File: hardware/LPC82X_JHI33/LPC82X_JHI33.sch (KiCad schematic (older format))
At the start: 24 parts, among them J1 LPC82XJHI33_LEFT, J2 LPC82XJHI33_RIGHT, J3 JTAG_2X05, U1 LPC824M201JHI33, Y1 12MHz

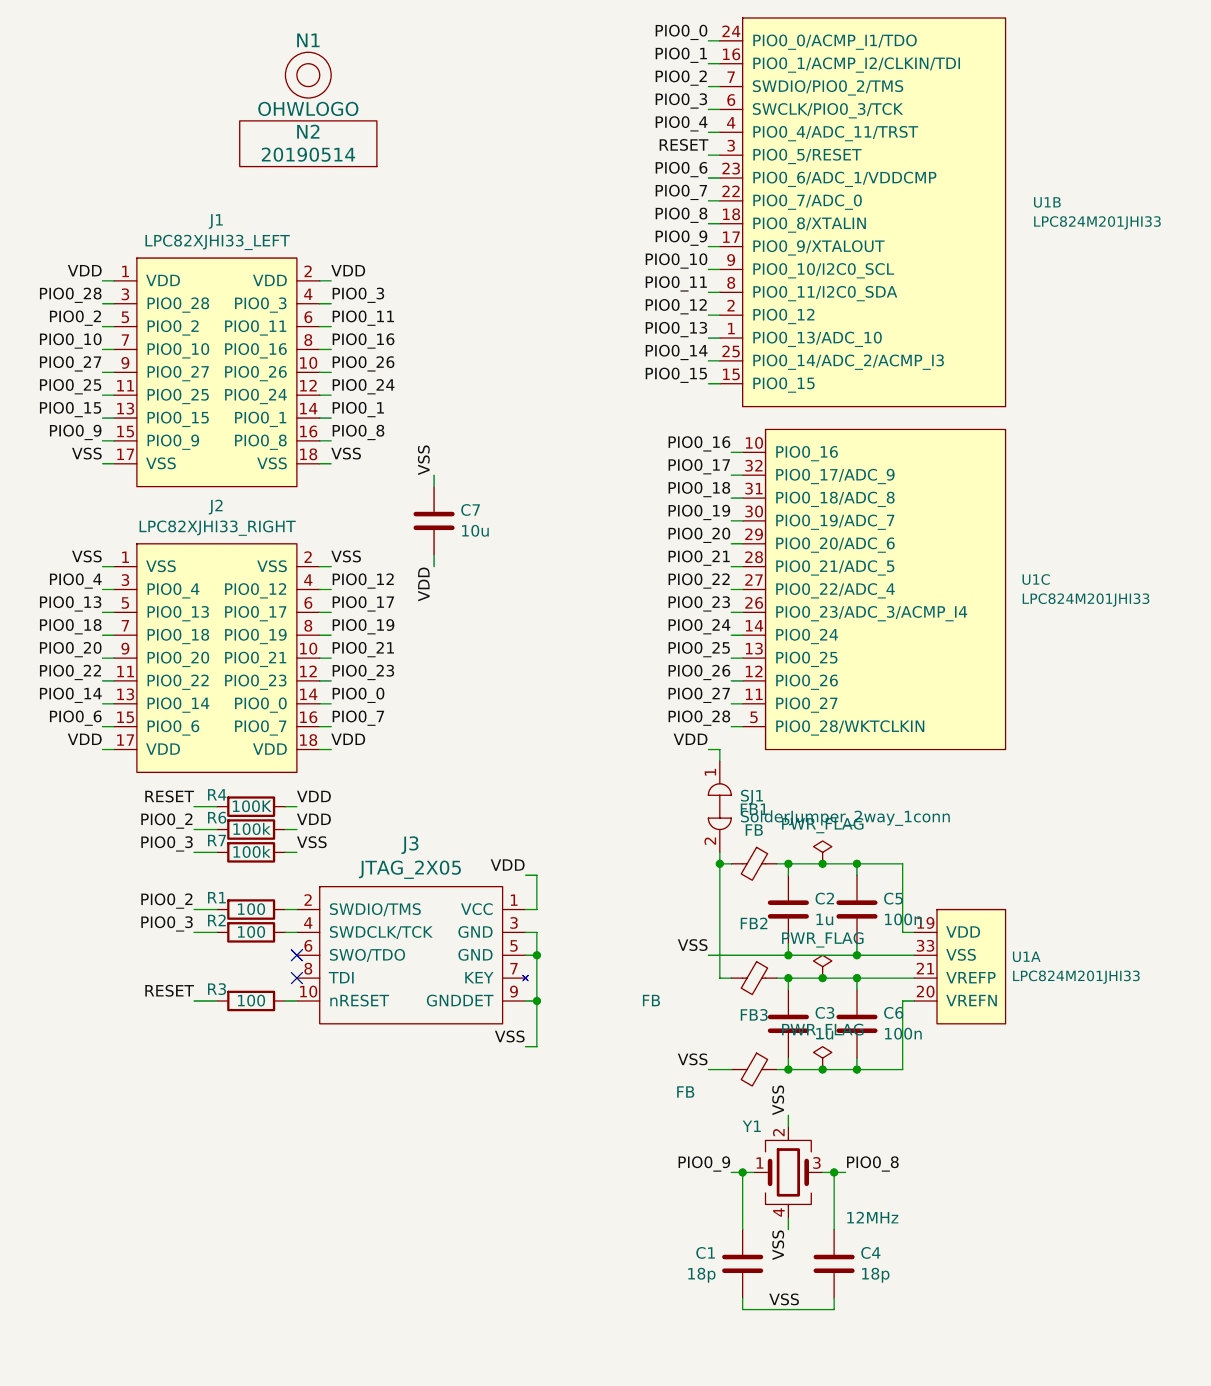
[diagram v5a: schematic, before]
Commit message: moved SWD connector to a subschematic
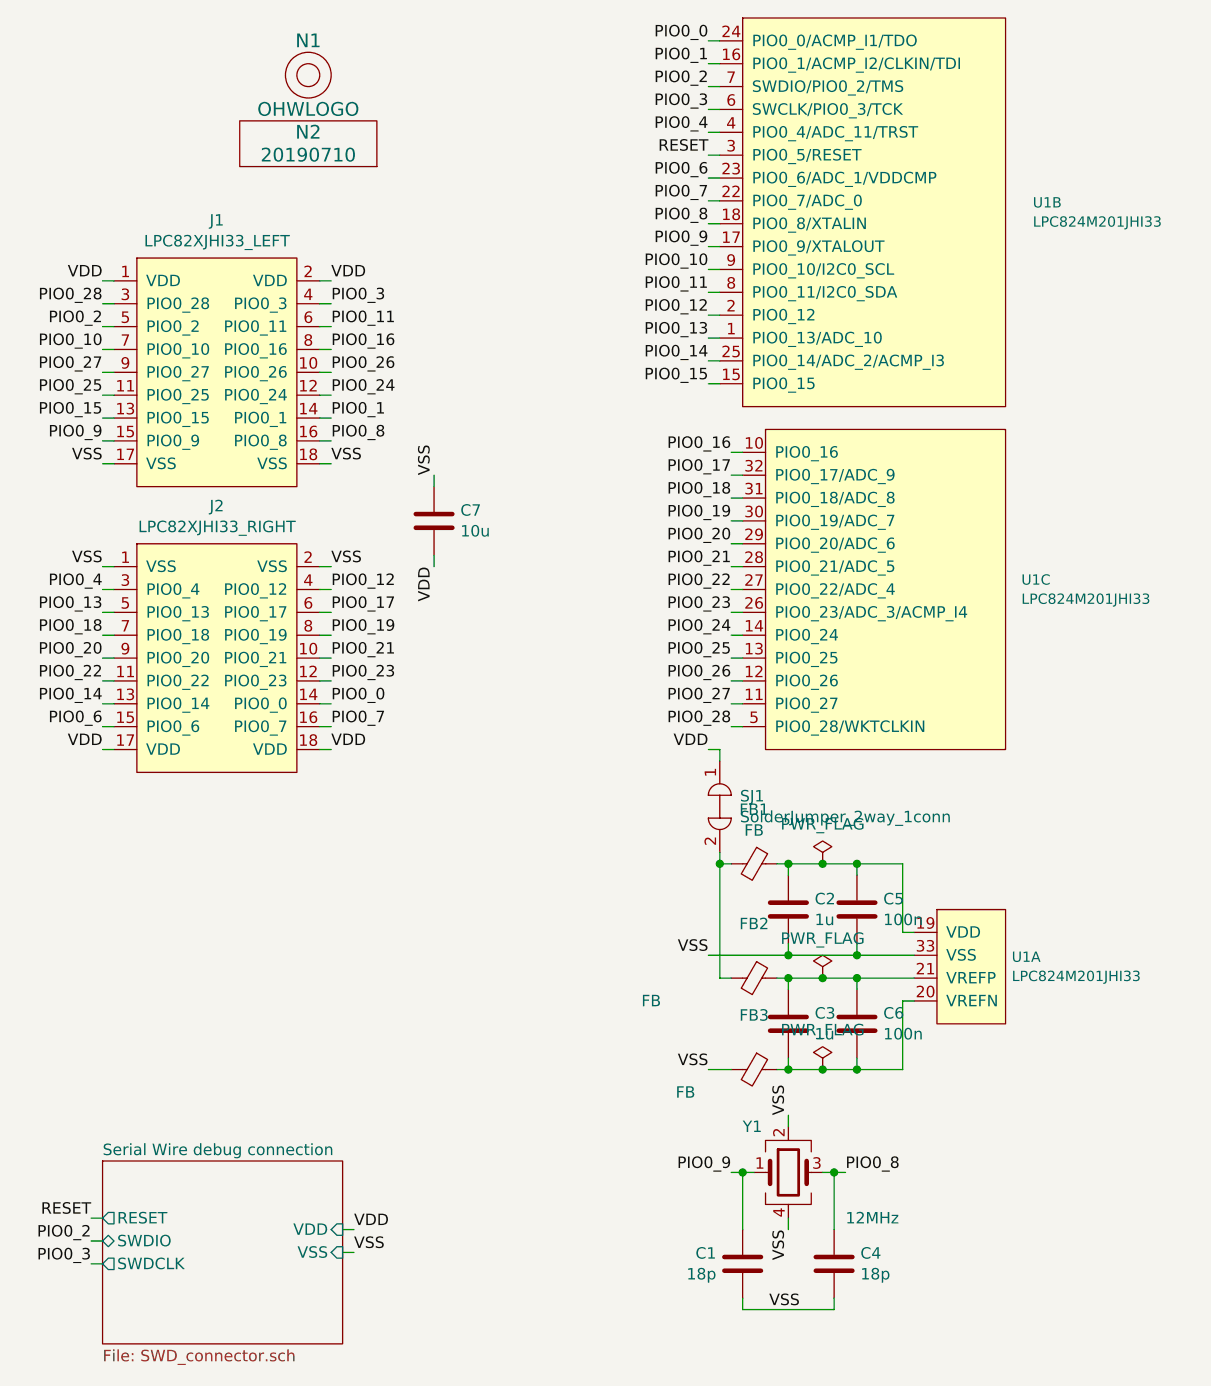
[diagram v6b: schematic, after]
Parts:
- removed J3: JTAG_2X05, SquantorConnectors:Header-0127-2X05-H006, symbol SquantorConnectors:JTAG_2X05
- removed R1, R2, R3: 100, SquantorRcl:R_0402_hand, symbol Device:R
- removed R4: 100K, SquantorRcl:R_0402_hand, symbol Device:R
- removed R6, R7: 100k, SquantorRcl:R_0402_hand, symbol Device:R
- N2: value 20190514 -> 20190710
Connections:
- no-connect marks 2 -> 0
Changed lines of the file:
@@
 $Descr A4 11693 8268
 encoding utf-8
-Sheet 1 1
+Sheet 1 2
 Title ""
 Date ""
@@
 P 4000 1650
 F 0 "N2" H 4000 1750 60  0000 C CNN
-F 1 "20190514" H 4000 1650 60  0000 C CNN
+F 1 "20190710" H 4000 1650 60  0000 C CNN
 F 2 "SquantorLabels:Label_version" H 4000 1650 60  0001 C CNN
 F 3 "" H 4000 1650 60  0001 C CNN
@@
 Wire Wire Line
 	4050 3450 4100 3450
-$Comp
-L SquantorConnectors:JTAG_2X05 J3
-U 1 1 5BD303CB
-P 4450 5150
-F 0 "J3" H 4450 5637 60  0000 C CNN
-F 1 "JTAG_2X05" H 4450 5531 60  0000 C CNN
-F 2 "SquantorConnectors:Header-0127-2X05-H006" H 4450 5300 60  0001 C CNN
-F 3 "" H 4450 5300 60  0001 C CNN
-	1    4450 5150
-	1    0    0    -1
-$EndComp
-Wire Wire Line
-	4950 5050 5000 5050
-Wire Wire Line
-	5000 5050 5000 5150
-Wire Wire Line
-	4950 5350 5000 5350
-Connection ~ 5000 5350
-Wire Wire Line
-	4950 5150 5000 5150
-Connection ~ 5000 5150
-Wire Wire Line
-	5000 5150 5000 5350
-Wire Wire Line
-	4950 4950 5000 4950
-$Comp
-L Device:R R1
-U 1 1 5BD32184
-P 3750 4950
-F 0 "R1" V 3700 4800 50  0000 C CNN
-F 1 "100" V 3750 4950 50  0000 C CNN
-F 2 "SquantorRcl:R_0402_hand" V 3680 4950 50  0001 C CNN
-F 3 "~" H 3750 4950 50  0001 C CNN
-	1    3750 4950
-	0    1    1    0
-$EndComp
-$Comp
-L Device:R R2
-U 1 1 5BD3223D
-P 3750 5050
-F 0 "R2" V 3700 4900 50  0000 C CNN
-F 1 "100" V 3750 5050 50  0000 C CNN
-F 2 "SquantorRcl:R_0402_hand" V 3680 5050 50  0001 C CNN
-F 3 "~" H 3750 5050 50  0001 C CNN
-	1    3750 5050
-	0    1    1    0
-$EndComp
-Wire Wire Line
-	3950 4950 3900 4950
-Wire Wire Line
-	3900 5050 3950 5050
-Wire Wire Line
-	3600 5050 3500 5050
-Wire Wire Line
-	3600 4950 3500 4950
-Text Label 3500 4950 2    50   ~ 0
-PIO0_2
-Text Label 3500 5050 2    50   ~ 0
-PIO0_3
-$Comp
-L Device:R R3
-U 1 1 5BD34D15
-P 3750 5350
-F 0 "R3" V 3700 5200 50  0000 C CNN
-F 1 "100" V 3750 5350 50  0000 C CNN
-F 2 "SquantorRcl:R_0402_hand" V 3680 5350 50  0001 C CNN
-F 3 "~" H 3750 5350 50  0001 C CNN
-	1    3750 5350
-	0    1    1    0
-$EndComp
-Wire Wire Line
-	3950 5350 3900 5350
-Wire Wire Line
-	3600 5350 3500 5350
-Text Label 3500 5350 2    50   ~ 0
-RESET
 Text Label 5750 1650 2    50   ~ 0
 RESET
@@
 	6100 6350 6100 6300
 $Comp
-L Device:R R7
-U 1 1 5BECCB56
-P 3750 4700
-F 0 "R7" V 3700 4550 50  0000 C CNN
-F 1 "100k" V 3750 4700 50  0000 C CNN
-F 2 "SquantorRcl:R_0402_hand" V 3680 4700 50  0001 C CNN
-F 3 "~" H 3750 4700 50  0001 C CNN
-	1    3750 4700
-	0    1    1    0
-$EndComp
-$Comp
-L Device:R R6
-U 1 1 5BECCC51
-P 3750 4600
-F 0 "R6" V 3700 4450 50  0000 C CNN
-F 1 "100k" V 3750 4600 50  0000 C CNN
-F 2 "SquantorRcl:R_0402_hand" V 3680 4600 50  0001 C CNN
-F 3 "~" H 3750 4600 50  0001 C CNN
-	1    3750 4600
-	0    1    1    0
-$EndComp
-Wire Wire Line
-	3950 4700 3900 4700
-Wire Wire Line
-	3900 4600 3950 4600
-Text Label 3500 4700 2    50   ~ 0
-PIO0_3
-Text Label 3500 4600 2    50   ~ 0
-PIO0_2
-Wire Wire Line
-	3600 4700 3500 4700
-Wire Wire Line
-	3600 4600 3500 4600
-$Comp
 L Device:Crystal_GND24 Y1
 U 1 1 5BE1D5EF
@@
 Text Label 6350 6100 0    50   ~ 0
 PIO0_8
-$Comp
-L Device:R R4
-U 1 1 5BD88002
-P 3750 4500
-F 0 "R4" V 3700 4350 50  0000 C CNN
-F 1 "100K" V 3750 4500 50  0000 C CNN
-F 2 "SquantorRcl:R_0402_hand" V 3680 4500 50  0001 C CNN
-F 3 "~" H 3750 4500 50  0001 C CNN
-	1    3750 4500
-	0    1    1    0
-$EndComp
-Text Label 3500 4500 2    50   ~ 0
-RESET
-Wire Wire Line
-	3500 4500 3600 4500
-Wire Wire Line
-	3900 4500 3950 4500
 Wire Wire Line
 	5800 5250 5800 4750
@@
 Text Label 4550 3450 3    50   ~ 0
 VDD
-Text Label 3950 4500 0    50   ~ 0
-VDD
-Text Label 3950 4600 0    50   ~ 0
-VDD
-Text Label 3950 4700 0    50   ~ 0
-VSS
-Text Label 4950 4800 2    50   ~ 0
-VDD
-Wire Wire Line
-	5000 4800 4950 4800
-Wire Wire Line
-	5000 4800 5000 4950
-Text Label 4950 5550 2    50   ~ 0
-VSS
-Wire Wire Line
-	4950 5550 5000 5550
-Wire Wire Line
-	5000 5350 5000 5550
 Text Label 5750 5150 2    50   ~ 0
 VSS
@@
 Wire Wire Line
 	6250 5650 6100 5650
-NoConn ~ 3950 5250
-NoConn ~ 3950 5150
+$Sheet
+S 3100 6050 1050 800
+U 5D27243C
+F0 "Serial Wire debug connection" 50
+F1 "SWD_connector.sch" 50
+F2 "RESET" O L 3100 6300 50
+F3 "SWDIO" B L 3100 6400 50
+F4 "SWDCLK" O L 3100 6500 50
+F5 "VDD" I R 4150 6350 50
+F6 "VSS" I R 4150 6450 50
+$EndSheet
+Text Label 3050 6300 2    50   ~ 0
+RESET
+Text Label 3050 6400 2    50   ~ 0
+PIO0_2
+Text Label 3050 6500 2    50   ~ 0
+PIO0_3
+Wire Wire Line
+	3100 6300 3050 6300
+Wire Wire Line
+	3050 6400 3100 6400
+Wire Wire Line
+	3050 6500 3100 6500
+Text Label 4200 6450 0    50   ~ 0
+VSS
+Text Label 4200 6350 0    50   ~ 0
+VDD
+Wire Wire Line
+	4150 6450 4200 6450
+Wire Wire Line
+	4200 6350 4150 6350
 $EndSCHEMATC
